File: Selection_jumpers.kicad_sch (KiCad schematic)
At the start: 7 parts, among them J10 U2RS485_TX, J17 U2RS485_DE_~{RE}, J17 U2RS485_RX, J6 R4_TX, J7 R4_RX

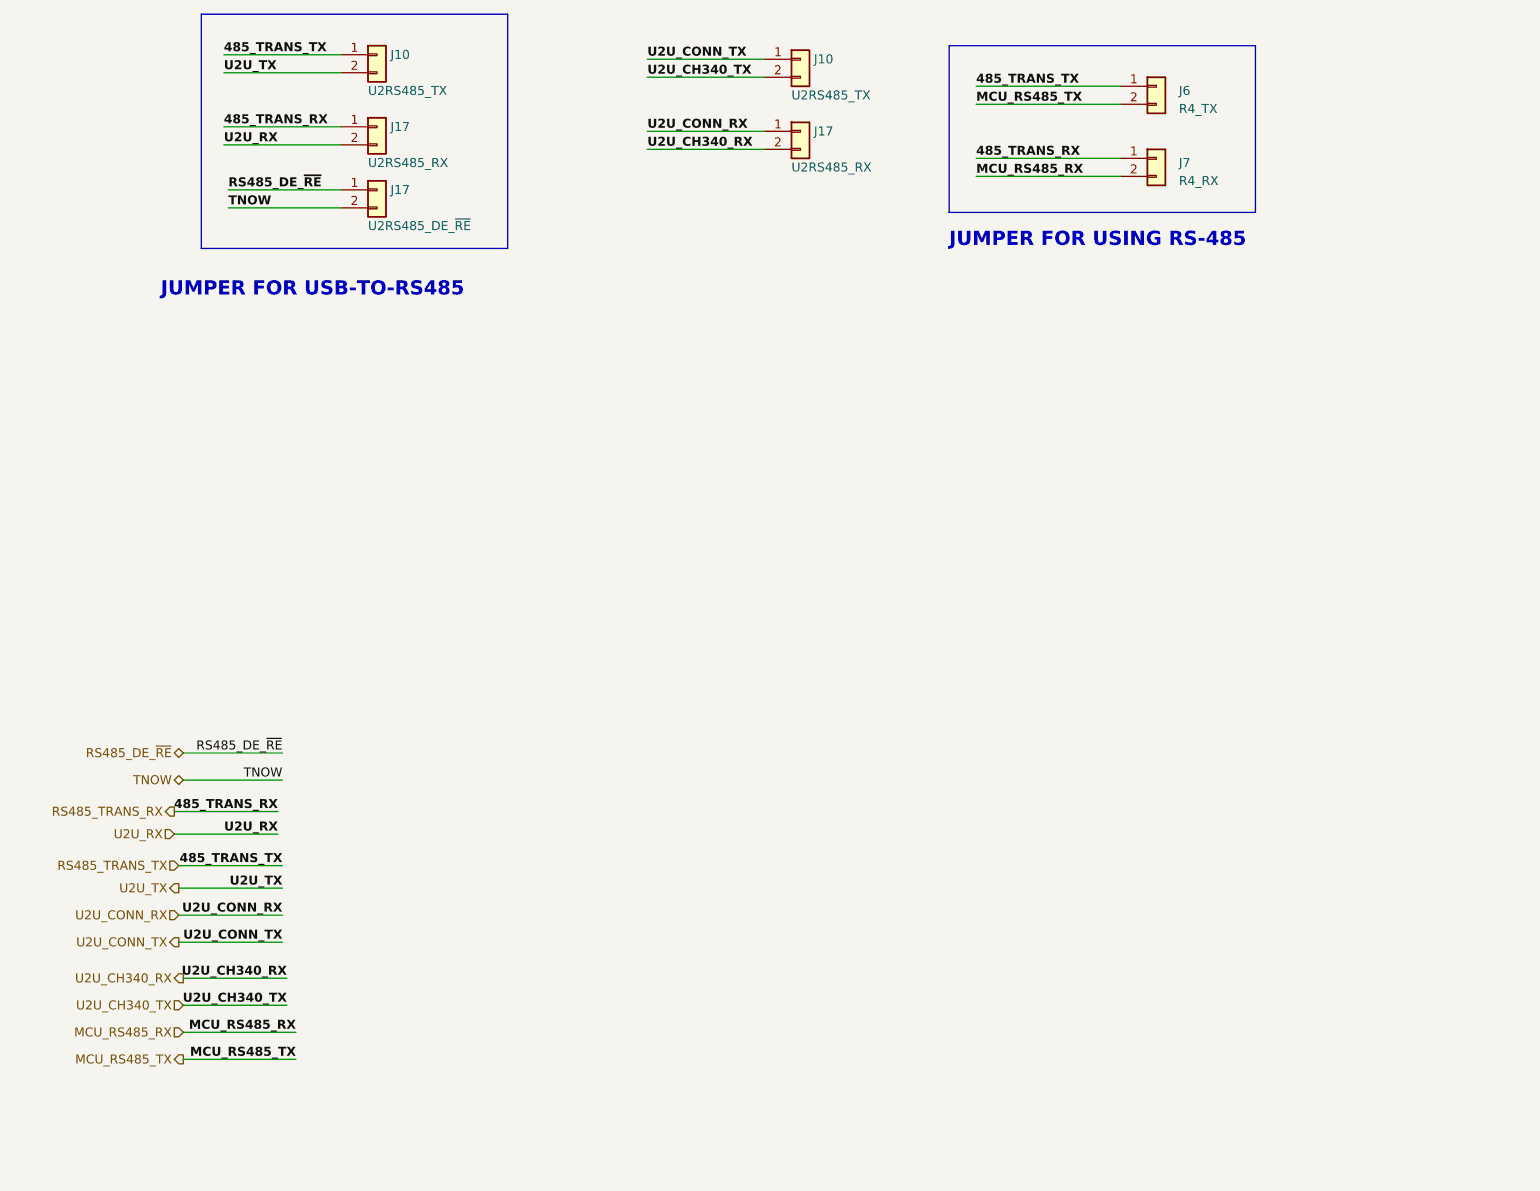
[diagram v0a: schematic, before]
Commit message: Added selection jumper block diagram and solved DRC errors
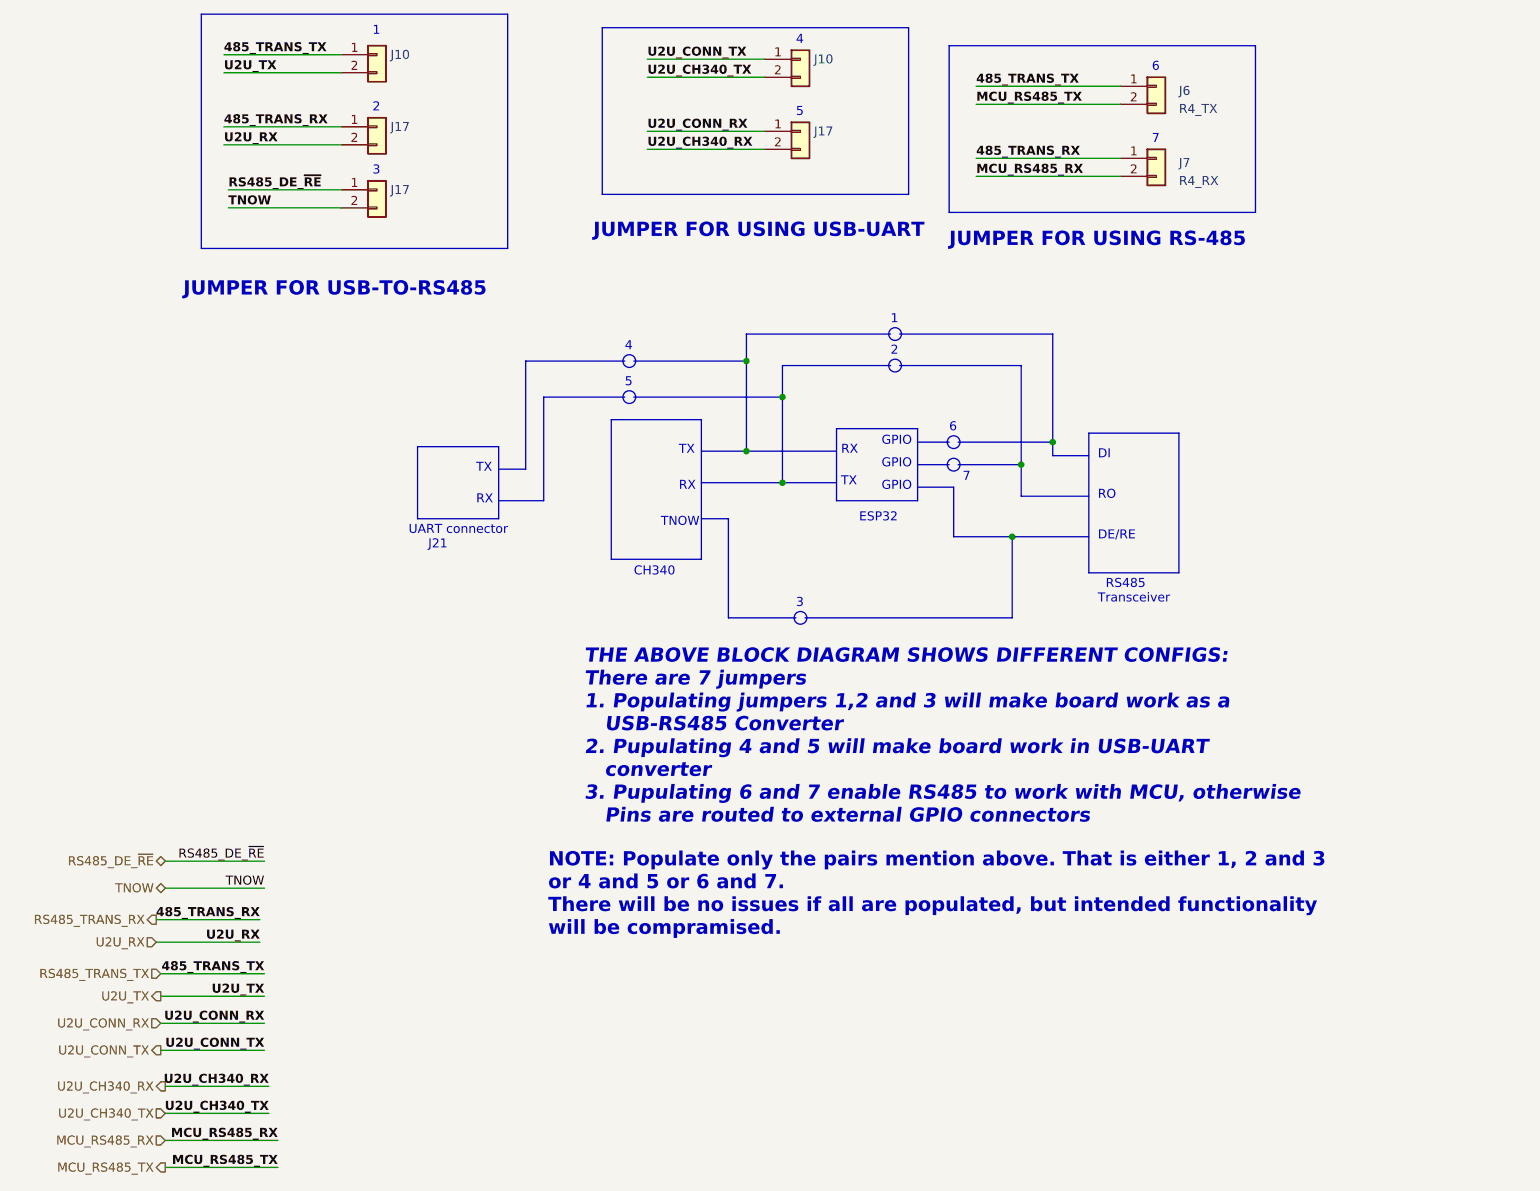
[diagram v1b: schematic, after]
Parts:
- J10: value U2RS485_TX -> U2U_TX
- J17: value U2RS485_RX -> U2U_RX
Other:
- note added: "1"
- note added: "2"
- note added: "3"
- note added: "4"
- note added: "5"
- note added: "6"
- note added: "7"
- note added: "CH340"
- note added: "DE/RE"
- note added: "DI"
- note added: "ESP32"
- note added: "GPIO"
- note added: "JUMPER FOR USING USB-UART"
- note added: "NOTE: Populate only the pairs mention above. That is either 1, 2 and 3 or 4 and 5 or 6 and 7. There will be no issues if all are populated, but intended functionality will be compramised."
- note added: "RO"
- note added: "RS485 Transceiver"
- note added: "RX"
- note added: "THE ABOVE BLOCK DIAGRAM SHOWS DIFFERENT CONFIGS: There are 7 jumpers 1. Populating jumpers 1,2 and 3 will make board work as a USB-RS485 Converter 2. Pupulating 4 and 5 will make board work in USB-UART converter 3. Pupulating 6 and 7 enable RS485 to work with MCU, otherwise Pins are routed to external GPIO connectors"
- note added: "TNOW"
- note added: "TX"
- note added: "UART connector J21"
